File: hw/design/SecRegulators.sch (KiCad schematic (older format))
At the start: 0 parts

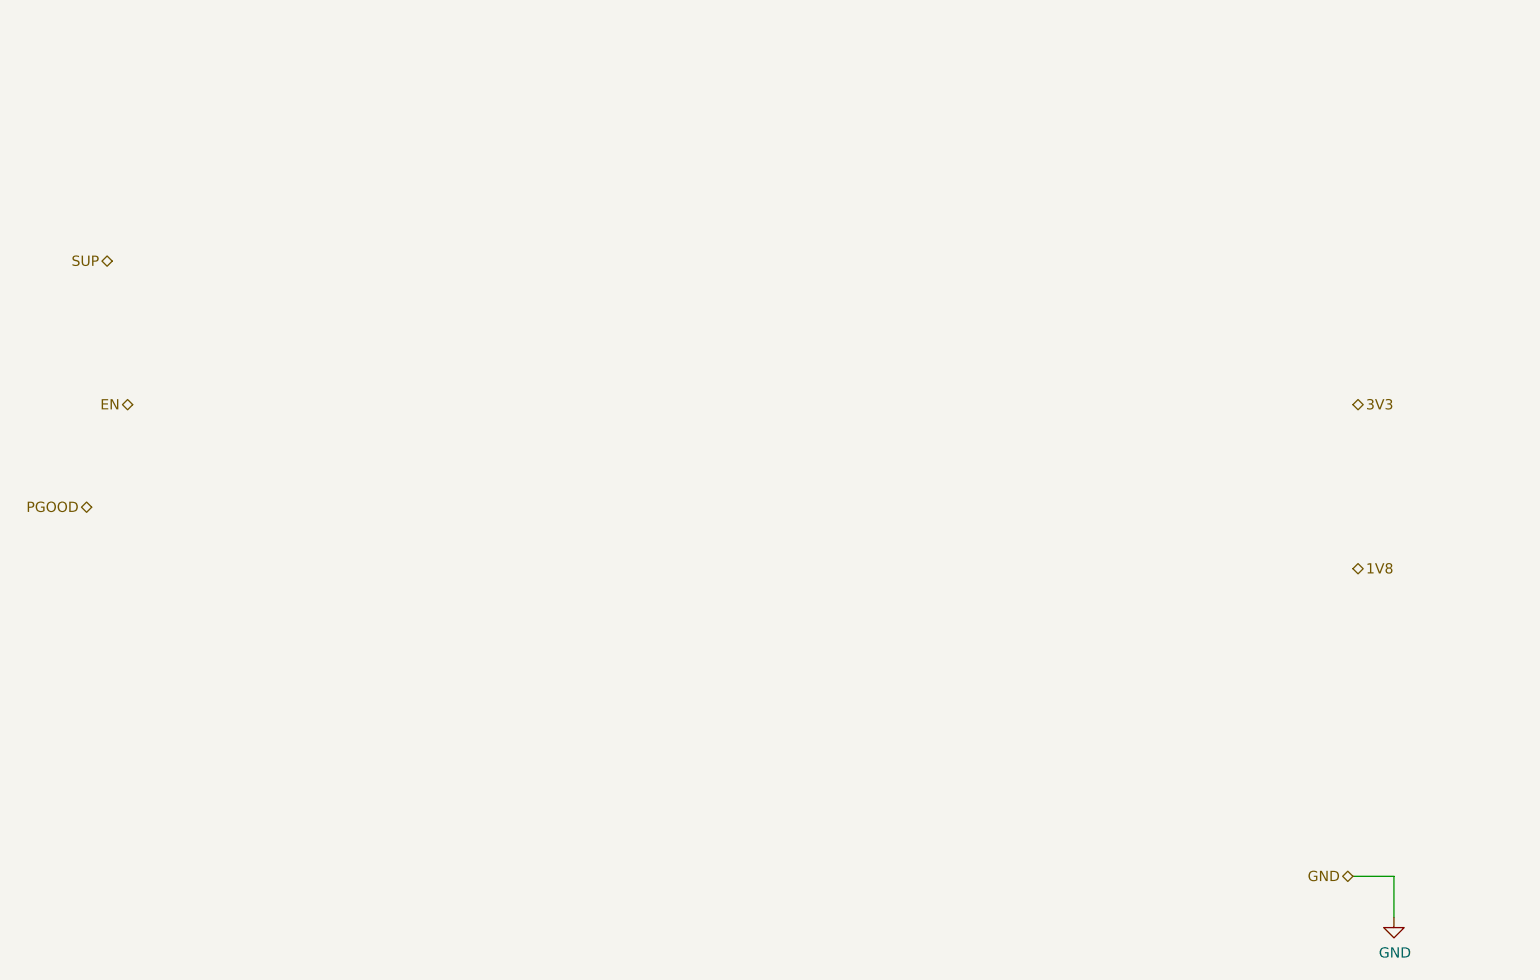
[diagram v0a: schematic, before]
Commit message: lots of work
expanded README doc, specifications, added secondary regulator circuit + symbol, more component specs added
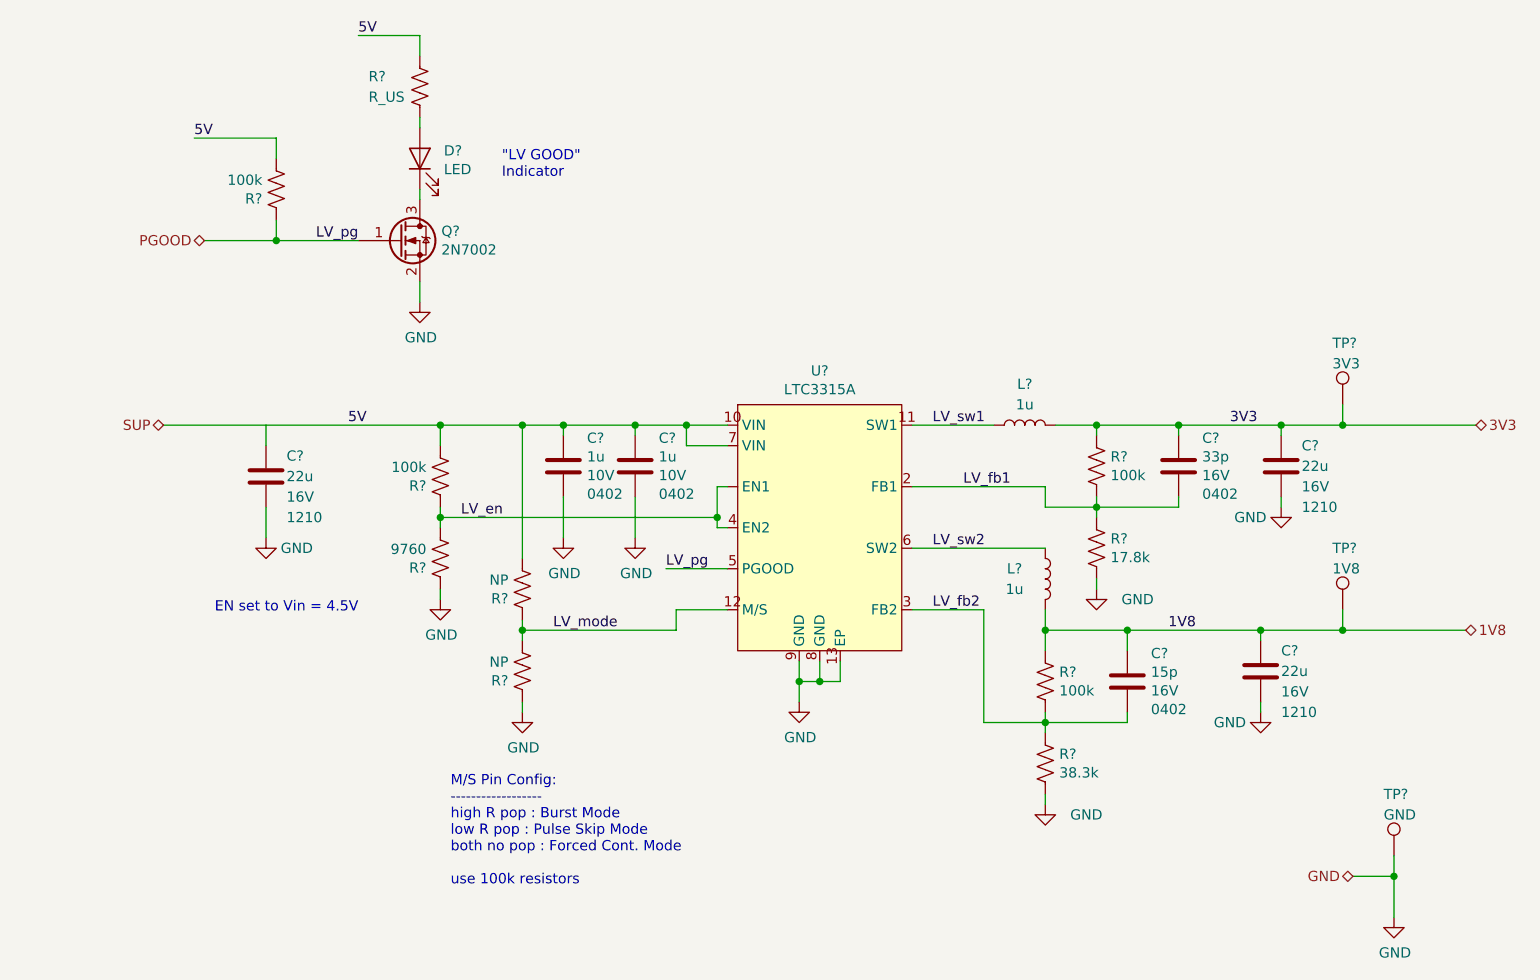
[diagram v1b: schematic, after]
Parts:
- added C? (x2): 1u, Capacitor_SMD:C_0603_1608Metric, symbol Device:C
- added C? (x3): 22u, Capacitor_SMD:C_1210_3225Metric_Pad1.42x2.65mm_HandSolder, symbol Device:C
- added C?: 33p, Capacitor_SMD:C_0603_1608Metric, symbol Device:C
- added C?: 15p, Capacitor_SMD:C_0603_1608Metric, symbol Device:C
- added D?: LED, LED_SMD:LED_0603_1608Metric, symbol Device:LED
- added L? (x2): 1u, symbol Device:L
- added Q?: 2N7002, Package_TO_SOT_SMD:SOT-323_SC-70, symbol Device:Q_NMOS_GSD
- added R?: 9760, Resistor_SMD:R_0603_1608Metric, symbol Device:R_US
- added R? (x4): 100k, Resistor_SMD:R_0603_1608Metric, symbol Device:R_US
- added R? (x2): NP, Resistor_SMD:R_0603_1608Metric, symbol Device:R_US
- added R?: R_US, Resistor_SMD:R_0603_1608Metric, symbol Device:R_US
- added R?: 17.8k, Resistor_SMD:R_0603_1608Metric, symbol Device:R_US
- added R?: 38.3k, Resistor_SMD:R_0603_1608Metric, symbol Device:R_US
- added TP?: 3V3, TestPoint:TestPoint_Keystone_5000-5004_Miniature, symbol Connector:TestPoint
- added TP?: 1V8, TestPoint:TestPoint_Keystone_5000-5004_Miniature, symbol Connector:TestPoint
- added TP?: GND, TestPoint:TestPoint_Keystone_5000-5004_Miniature, symbol Connector:TestPoint
- added U?: LTC3315A, symbol pps_klib:LTC3315A
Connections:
- net 1V8: now also C?.1, C?.1, L?.2, R?.1, TP?.1
- net 3V3: now also C?.1, C?.1, L?.2, R?.1, TP?.1
- net GND: now also C?.2, C?.2, C?.2, C?.2, C?.2, Q?.2 (S), R?.1, R?.1, R?.2, R?.2, TP?.1, U?.13 (EP), U?.8 (GND), U?.9 (GND)
- net PGOOD: now also Q?.1 (G), R?.1, U?.5 (PGOOD)
- net SUP: now also C?.1, C?.1, R?.1, R?.2, R?.2, R?.2, U?.10 (VIN), U?.7 (VIN)
- new net: D?.1 (K), Q?.3 (D)
- new net: D?.2 (A), R?.2
- new net LV_en: R?.1, R?.2, U?.4 (EN2), U?.~ (EN1)
- new net LV_fb1: C?.2, R?.1, R?.2, U?.2 (FB1)
- new net LV_fb2: C?.2, R?.1, R?.2, U?.3 (FB2)
- new net LV_mode: R?.1, R?.2, U?.12 (M/S)
- new net LV_sw1: L?.1, U?.11 (SW1)
- new net LV_sw2: L?.1, U?.6 (SW2)
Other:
- note added: ""LV GOOD"\nIndicator"
- note added: "EN set to Vin = 4.5V\n\n"
- note added: "M/S Pin Config:\n------------------\nhigh R pop : Burst Mode\nlow R pop : Pulse Skip Mode\nboth no pop : Forced Cont. Mode\n\nuse 100k resistors"

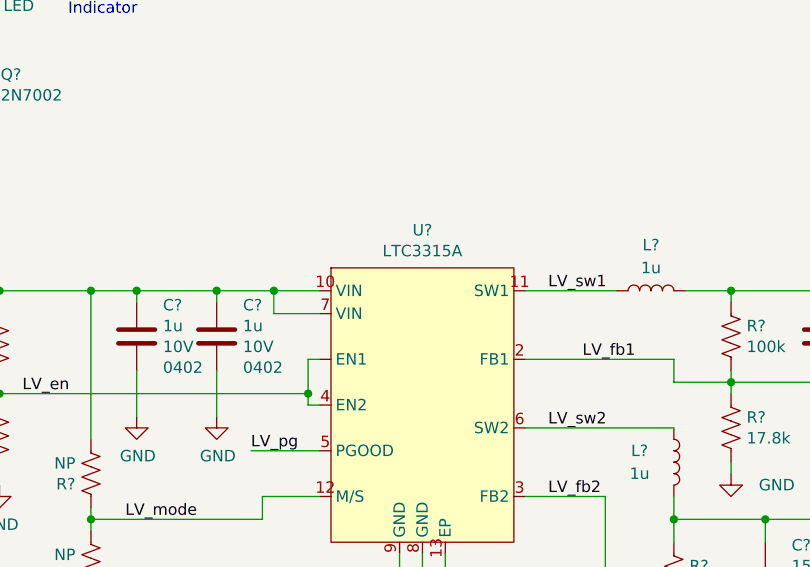
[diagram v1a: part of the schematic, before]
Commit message: more part numbers
Added manfacturer part numbers to ICs, added descriptions to symbols in library
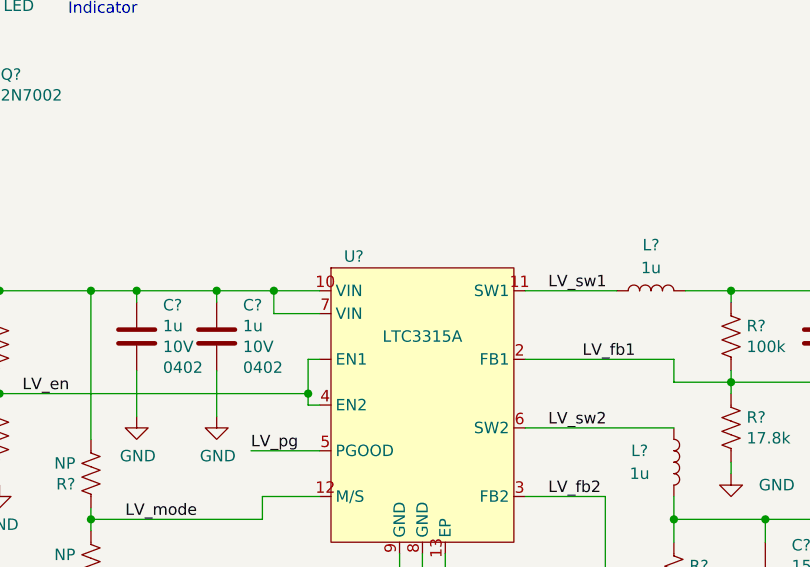
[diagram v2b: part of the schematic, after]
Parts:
- U?: MfrNum (none) -> ADI_LTC3315AEV
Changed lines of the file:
@@
 U 1 1 5EC9E852
 P 5100 3300
-F 0 "U?" H 5100 4065 50  0000 C CNN
-F 1 "LTC3315A" H 5100 3974 50  0000 C CNN
+F 0 "U?" H 4800 3950 50  0000 C CNN
+F 1 "LTC3315A" H 5100 3600 50  0000 C CNN
 F 2 "" H 5100 3300 50  0001 C CNN
 F 3 "" H 5100 3300 50  0001 C CNN
+F 4 "ADI_LTC3315AEV" H 5100 3300 50  0001 C CNN "MfrNum"
 	1    5100 3300
 	1    0    0    -1
